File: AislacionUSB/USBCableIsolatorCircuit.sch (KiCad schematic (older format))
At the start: 65 parts, among them CON1 BARREL_JACK, J1 MICRO_USB, J2 TB_1X2, P1 USB_B, U1 PRTR5V0U2X, U2 ADUM5000, U3 ADUM4160, U4 PRTR5V0U2X, U5 7805

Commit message: Aislacion USB - Datos componentes en el SCH
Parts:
- removed C10, C11, C12, C13, C14, C15, C16, C17, C18, C19, C2, C20, C21, C22, C24, C3, C4, C5, C6, C7, C8, C9: C, symbol C
- removed FB2, FB3, FB4: FILTER, symbol FILTER
- removed JP1: JUMPER3, symbol JUMPER3
- removed R10, R3, R9: R, symbol R
- removed TR2: TRASF_UNIP, symbol TRASF_UNIP
- removed U4: PRTR5V0U2X, symbol PRTR5V0U2X
- added C? (x20): 100nF, Capacitors_SMD:C_0603_HandSoldering, symbol C
- added C? (x2): 100nF, Capacitors_SMD:C_1812_HandSoldering, symbol C
- added FB? (x3): MMZ1608B601C, fb_0603, symbol FILTER
- added JP?: JUMPER3, PIN_ARRAY_3x1, symbol JUMPER3
- added R? (x3): 24, Resistors_SMD:R_0603_HandSoldering, symbol R
- added TR?: SRF2012, SRF2012, symbol TRASF_UNIP
- added U?: PRTR5V0U2X, SOT-143-4, symbol PRTR5V0U2X
- C1: value C -> 100nF; footprint (none) -> Capacitors_SMD:C_0603_HandSoldering; Desc (none) -> CAP CER 0,1UF 16V X7R 10% 0603; Digikey# (none) -> 399-1096-1-ND; Manf (none) -> Kemet; Manf# (none) -> C0603C104K4RACTU
- FB1: value FILTER -> MMZ1608B601C; footprint (none) -> fb_0603; Desc (none) -> FERRITE CHIP 600 OHM 500MA 0603; Digikey# (none) -> 445-2166-1-ND; Manf (none) -> TDK; Manf# (none) -> MMZ1608B601C
- J1: footprint (none) -> USB_MicroAB; Descripcion CONNECTOR RECEPTACLE MICRO USB AB SMD -> CONNECTOR RECEPTACLE MICRO USB AB SMD BOTTOM MOUNT; Digikey# (none) -> H11635TR-ND; Manf (none) -> HIROSE ELECTRIC; Manf# (none) -> ZX62-AB-5PA(11)
- J2: value TB_1X2 -> IN_VCC; footprint (none) -> bornier2; Desc (none) -> TERM BLOCK 5.08MM VERT 2POS PCB; Digikey# (none) -> 571-7969492; Manf# (none) -> 796949-2
- JP?: footprint (none) -> PIN_ARRAY_3x1; Digikey# (none) -> JUMPER 3 TERM
- R1, R11: value R -> 400
- R2: value R -> 24; footprint (none) -> Resistors_SMD:R_0603_HandSoldering; Desc (none) -> RES SMD 24 OHM 5% 1/10W 0603; Digikey# (none) -> P24GTR-ND; Manf (none) -> Panasonic Electronic Components; Manf# (none) -> ERJ-3GEYJ240V
- TR1: value TRASF_UNIP -> SRF2012; footprint (none) -> SRF2012; Desc (none) -> INDUCTOR COMMON MODE 90 OHM SMD; Digikey# (none) -> SRF2012-900YCT-ND; Manf (none) -> BOURNS; Manf# (none) -> SRF2012-900Y
- U1: footprint (none) -> SOT-143-4; Desc (none) -> IC TVS DIODE 2 CHANNEL 10V CLAMP SOT1434; Digikey# (none) -> CM1213A-02SROSCT-ND; Manf (none) -> ON SEMICONDUCTOR; Manf# (none) -> CM1213A-02SR
- U2: Desc (none) -> IC DIG ISOLATOR W/DC-DC 16SOIC; Digikey# (none) -> ADUM5000ARWZ-RLCT-ND; Manf (none) -> Analog Devices Inc.; Manf# (none) -> ADUM5000ARWZ-RL
- U3: Desc (none) -> USB Digital Isolator 5000Vrms 2 Channel 12Mbps 25kV/µs CMTI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; Digikey# (none) -> ADUM4160BRWZ-RLTR-ND; Manf (none) -> Analog Devices Inc.; Manf# (none) -> ADUM4160BRWZ-RL
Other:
- moved on the sheet: JP2

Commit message: Se agrego una hoja jerarquica para el ADUM4160 - Se completaron los campos de los componentes
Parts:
- removed C? (x3): 100nF, Capacitors_SMD:C_0603_HandSoldering, symbol C
- removed D2: LED, symbol LED
- removed JP2: JUMPER3, symbol JUMPER3
- removed JP?: JUMPER3, PIN_ARRAY_3x1, symbol JUMPER3
- removed L1: INDUCTOR, symbol INDUCTOR
- removed P1: USB_B, symbol USB_B
- removed R1: 400, symbol R
- removed R4, R5, R6, R7, R8: R, symbol R
- removed U3: ADUM4160, symbol ADUM4160
- added D?: LED, LEDs:LED_0805, symbol LED
- added P?: USB_A, symbol USB_A
- added R?: 400, Resistors_SMD:R_0805_HandSoldering, symbol R
- C23: value CAPAPOL -> 10uF; footprint c_elec_13.7x13x13.5 -> Capacitors_Tantalum_SMD:TantalC_SizeA_EIA-3216_HandSoldering; Desc (none) -> 10µF Molded Tantalum - Polymer Capacitors 10V 1206 (3216 Me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; Digikey# (none) -> 399-4788-2-ND; Manf (none) -> Kemet; Manf# (none) -> T520A106M010ATE080
- CON1: footprint (none) -> Connect:JACK_ALIM; Desc (none) -> DC JACK W/SOLDER LUGS PCB MOUNT; Digikey# (none) -> EJ508A-ND; Manf (none) -> MPD; Manf# (none) -> EJ508A
- D1: footprint (none) -> LEDs:LED_0805; Desc (none) -> LED GREEN DIFFUSED 0805 SMD; Digikey# (none) -> 475-1410-2-ND; Manf (none) -> OSRAM; Manf# (none) -> LG R971-KN-1
- D3: value D_Schottky -> SMAJ5.0A; footprint (none) -> DO-214AC_SMA; Desc (none) -> TVS DIODE 5VWM SMD; Digikey# (none) -> SMAJ5.0ABCT-ND; Manf (none) -> Bourns; Manf# (none) -> SMAJ5.0A
- JP?: Desc (none) -> 3 Positions Header, Unshrouded Connector 0.100\" (2.54mm) T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; Digikey# JUMPER 3 TERM -> Z5375-ND; Manf (none) -> Omron Electronics; Manf# (none) -> XG8V-0331
- R11: footprint (none) -> Resistors_SMD:R_0805_HandSoldering; Desc (none) -> RES SMD 390 OHM 5% 1/8W 0805; Digikey# (none) -> P390ACT-ND; Manf (none) -> Panasonic Electronic Components; Manf# (none) -> ERJ-6GEYJ391V
- U5: footprint (none) -> Power_Integrations:TO-220; Desc (none) -> Linear Voltage Regulator IC Positive Fixed 1 Output 5V 1A T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; Digikey# (none) -> LM7805CT-ND; Manf (none) -> Fairchild Semiconductor; Manf# (none) -> LM7805CT
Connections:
- net labels removed: PIN, SPD, SPU, VDD1, VDD2
- wire segments 211 -> 163
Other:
- note removed: "Aislación de los datos"
- note removed: "Full Speed"
- note removed: "Low speed"

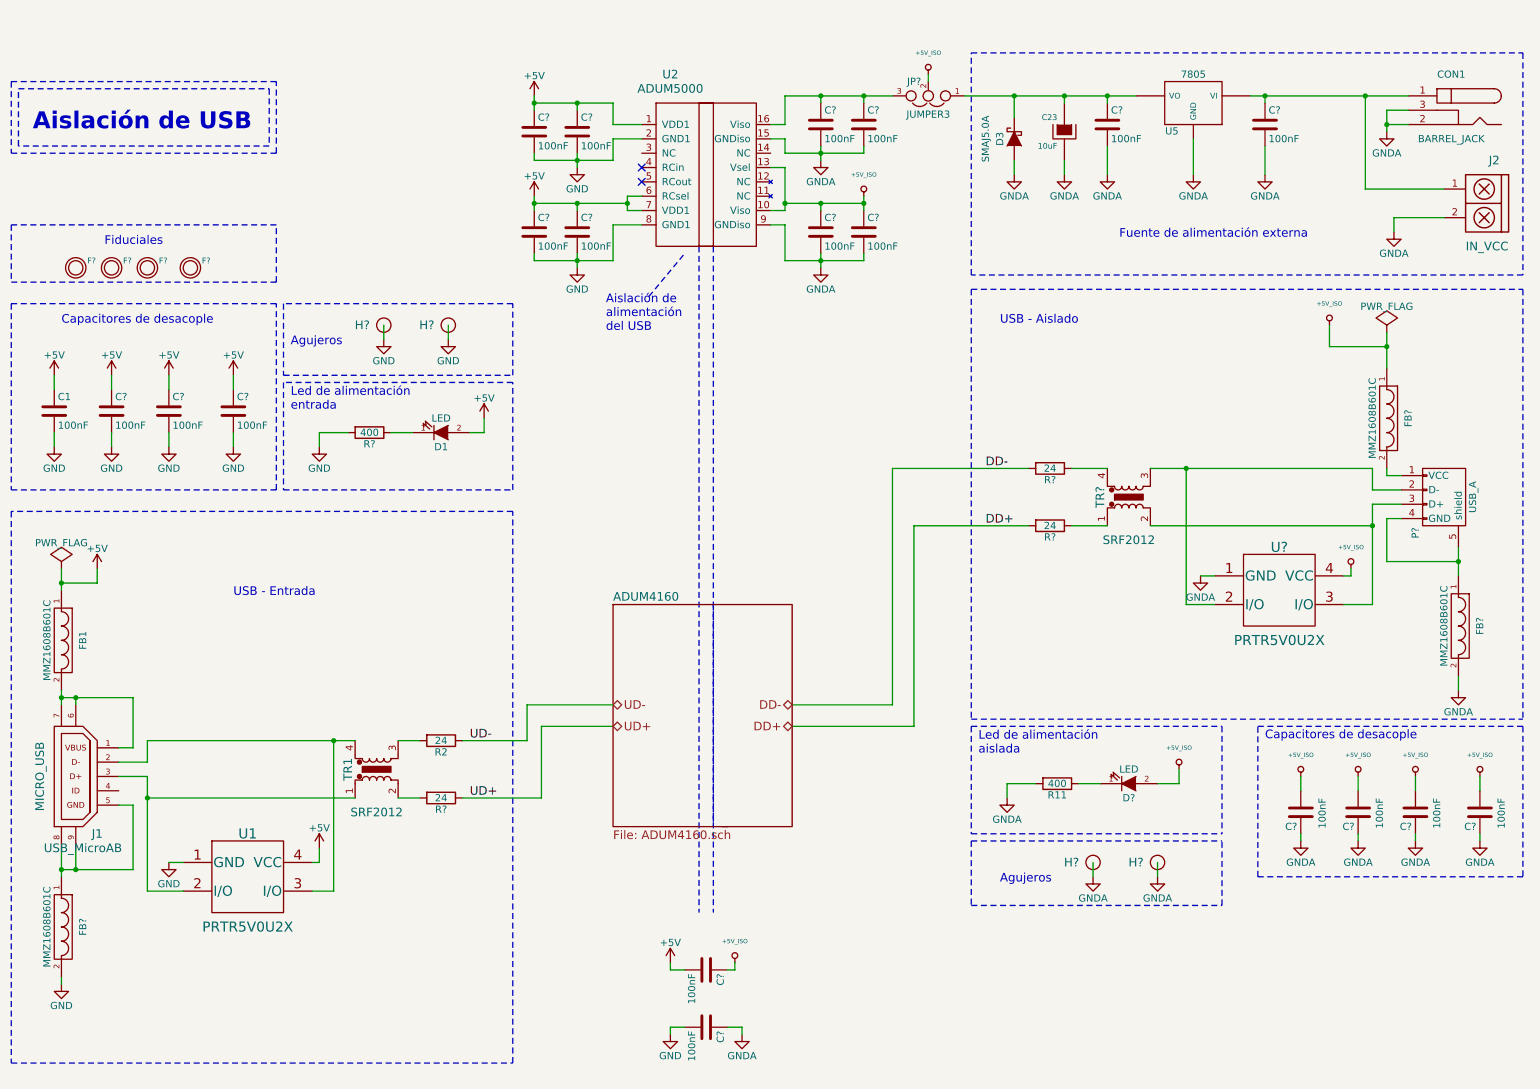
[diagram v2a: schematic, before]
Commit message: Se asociaron los footprints
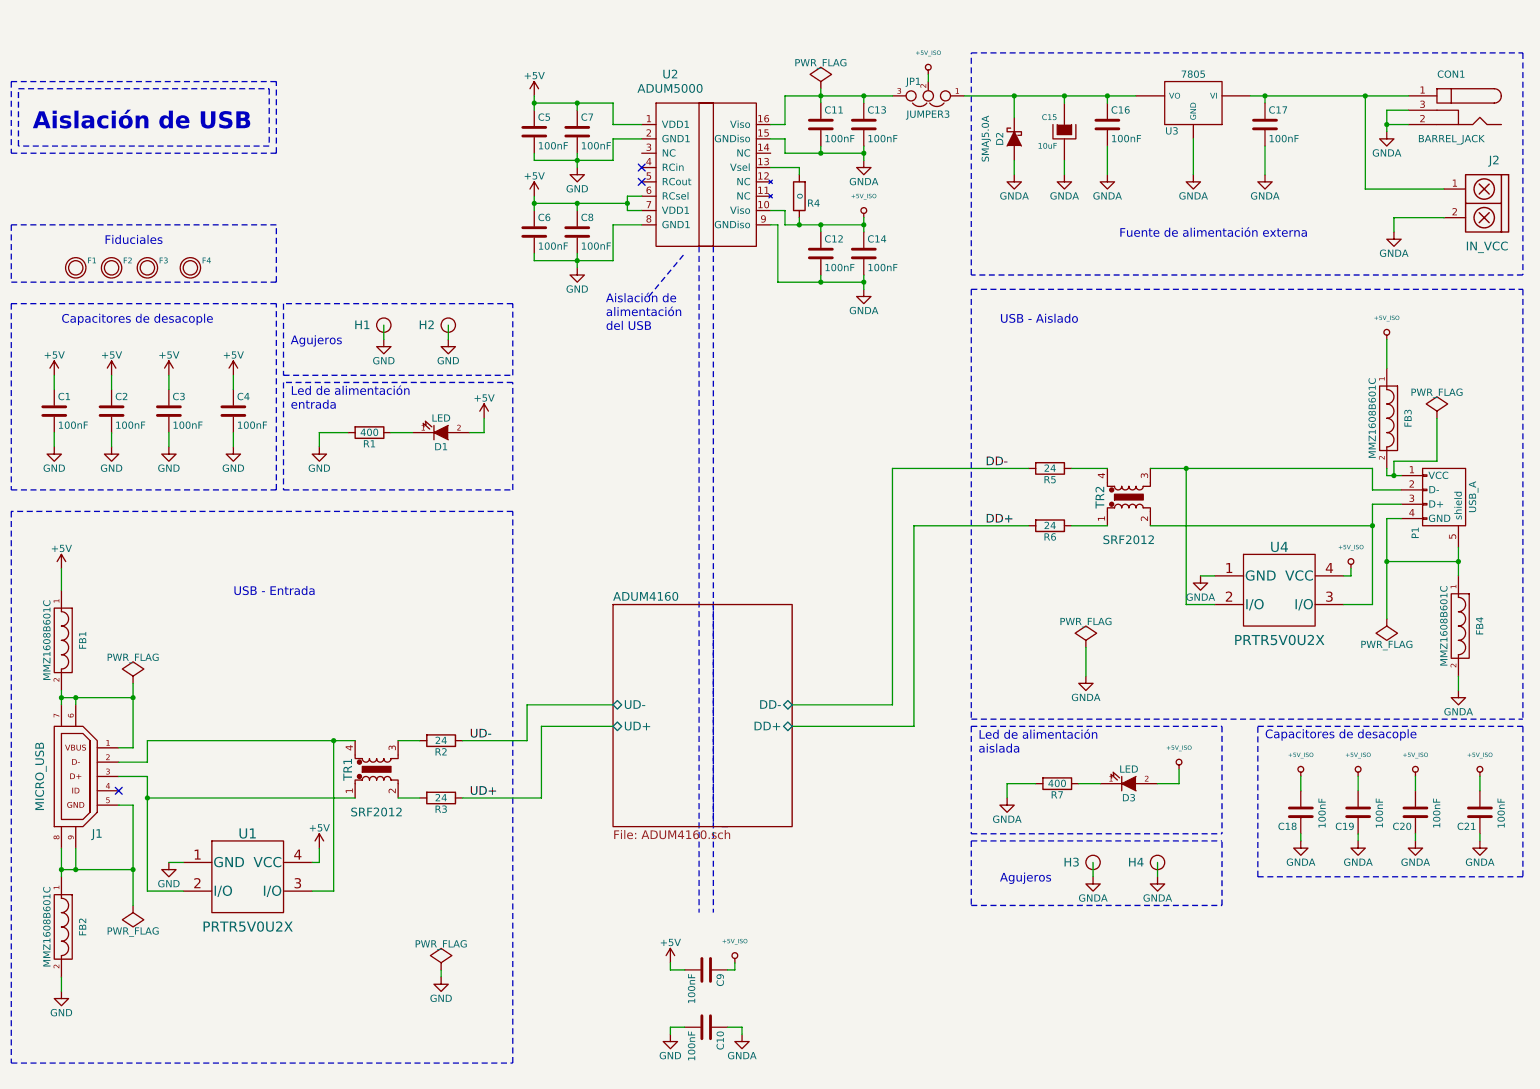
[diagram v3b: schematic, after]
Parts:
- added R4: o, Resistors_SMD:R_0603_HandSoldering, symbol R
- C15: renamed from C23; footprint Capacitors_Tantalum_SMD:TantalC_SizeA_EIA-3216_HandSoldering -> SMD_Packages:SMD-1206_Pol
- D2: renamed from D3; footprint DO-214AC_SMA -> Diodes_SMD:DO-214AB_Handsoldering
- F1, F2, F3, F4: renamed from F?; footprint (none) -> Fiducials:Fiducial_1mm_Dia_2.54mm_Outer_CopperBottom
- FB1: footprint fb_0603 -> Capacitors_SMD:C_0603_HandSoldering
- FB2, FB3, FB4: renamed from FB?; footprint fb_0603 -> Capacitors_SMD:C_0603_HandSoldering
- H1, H2, H3, H4: renamed from H?; footprint (none) -> Mounting_Holes:MountingHole_2.7mm
- J1: footprint USB_MicroAB -> AislacionUSB:USB_MicroAB
- J2: footprint bornier2 -> Connect:bornier2
- JP1: renamed from JP?; footprint PIN_ARRAY_3x1 -> Connect:PINHEAD1-3
- P1: renamed from P?; footprint (none) -> Connect:USB_A
- R2: footprint Resistors_SMD:R_0603_HandSoldering -> Resistors_SMD:R_0805_HandSoldering
- R3: renamed from R?; footprint Resistors_SMD:R_0603_HandSoldering -> Resistors_SMD:R_0805_HandSoldering
- TR1: footprint SRF2012 -> AislacionUSB:SRF2012
- TR2: renamed from TR?; footprint SRF2012 -> AislacionUSB:SRF2012
- U1: footprint SOT-143-4 -> AislacionUSB:SOT-143-4
- U2: footprint (none) -> Housings_SOIC:SOIC-16_7.5x10.3mm_Pitch1.27mm
- U4: renamed from U?; footprint SOT-143-4 -> AislacionUSB:SOT-143-4
- gave numbers to parts that had none: 23
- renumbered R11 to R7, U5 to U3
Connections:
- net +5V_iso: now also R4.1; no longer U2.13 (Vsel)
- new net: R4.2, U2.13 (Vsel)
- no-connect marks 2 -> 3
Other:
- moved on the sheet: C12, C14

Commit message: Rev01 – Se incorporaron las observaciones realizadas en la primera revisión del esquemático - doc:
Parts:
- C13, C14: value 100nF -> 10uF; footprint Capacitors_SMD:C_0603_HandSoldering -> Capacitors_SMD:C_1206_HandSoldering; Desc (none) -> 10 µF, 10 V, Capacitores cerámicos, X7R, 1206; Digikey# 399-1096-1-ND -> 445-1602-1-ND; Manf Kemet -> TDK Corporation; Manf# C0603C104K4RACTU -> C3216X7R1A106M160AC
- C5, C6: value 100nF -> 10uF; footprint Capacitors_SMD:C_0603_HandSoldering -> Capacitors_SMD:C_1206_HandSoldering; Desc CAP CER 0,1UF 16V X7R 10% 0603 -> 10 µF, 10 V, Capacitores cerámicos, X7R, 1206; Digikey# 399-1096-1-ND -> 445-1602-1-ND; Manf Kemet -> TDK Corporation; Manf# C0603C104K4RACTU -> C3216X7R1A106M160AC
- R1, R7: value 400 -> 390
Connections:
- net +5V_iso: no longer C12.1, C14.1, R4.1, U2.10 (Viso)
- net GND: now also U2.3 (NC)
- net GNDA: now also U2.14 (NC)
- net at C11.1, C13.1, JP1.3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: now also C12.1, C14.1, R4.1, U2.10 (Viso)
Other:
- moved on the sheet: C5, C7

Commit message: Datos fabricante
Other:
- note added: "Selecciona\nla\nAlimentacion"
- moved on the sheet: C11, C12, C13, C14, C5, C6, C7, C8, JP1, R4, U2
